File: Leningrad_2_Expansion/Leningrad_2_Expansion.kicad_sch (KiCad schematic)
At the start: 2 parts, among them J1 ZX_Spectrum_Connector_48K, X6 Leningrad 2 Expansion Bus

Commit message: Updated Leningrad-2 symbol
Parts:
- X6: value Leningrad 2 Expansion Bus -> Ленинград-2 Expansion Bus
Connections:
- net D5: no longer X6.A14 (D5)
- net D6: no longer X6.A15 (D6)
- net D7: no longer X6.A16 (D7)

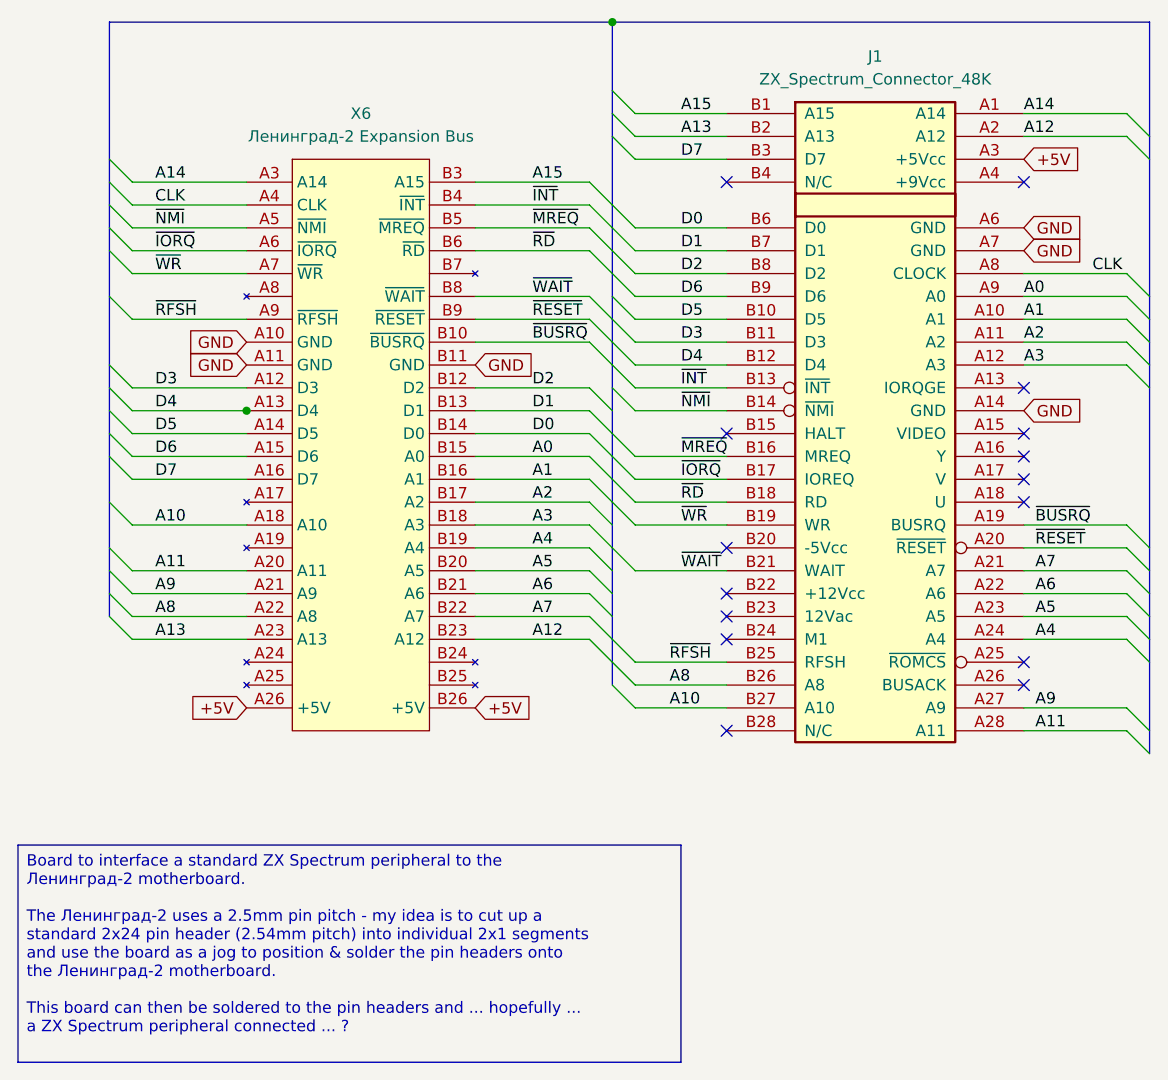
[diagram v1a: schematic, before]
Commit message: Added ~IORQGE signal
Thanks to Oleh S. suggestion on UCHC "Ukrainian Computing History Community"
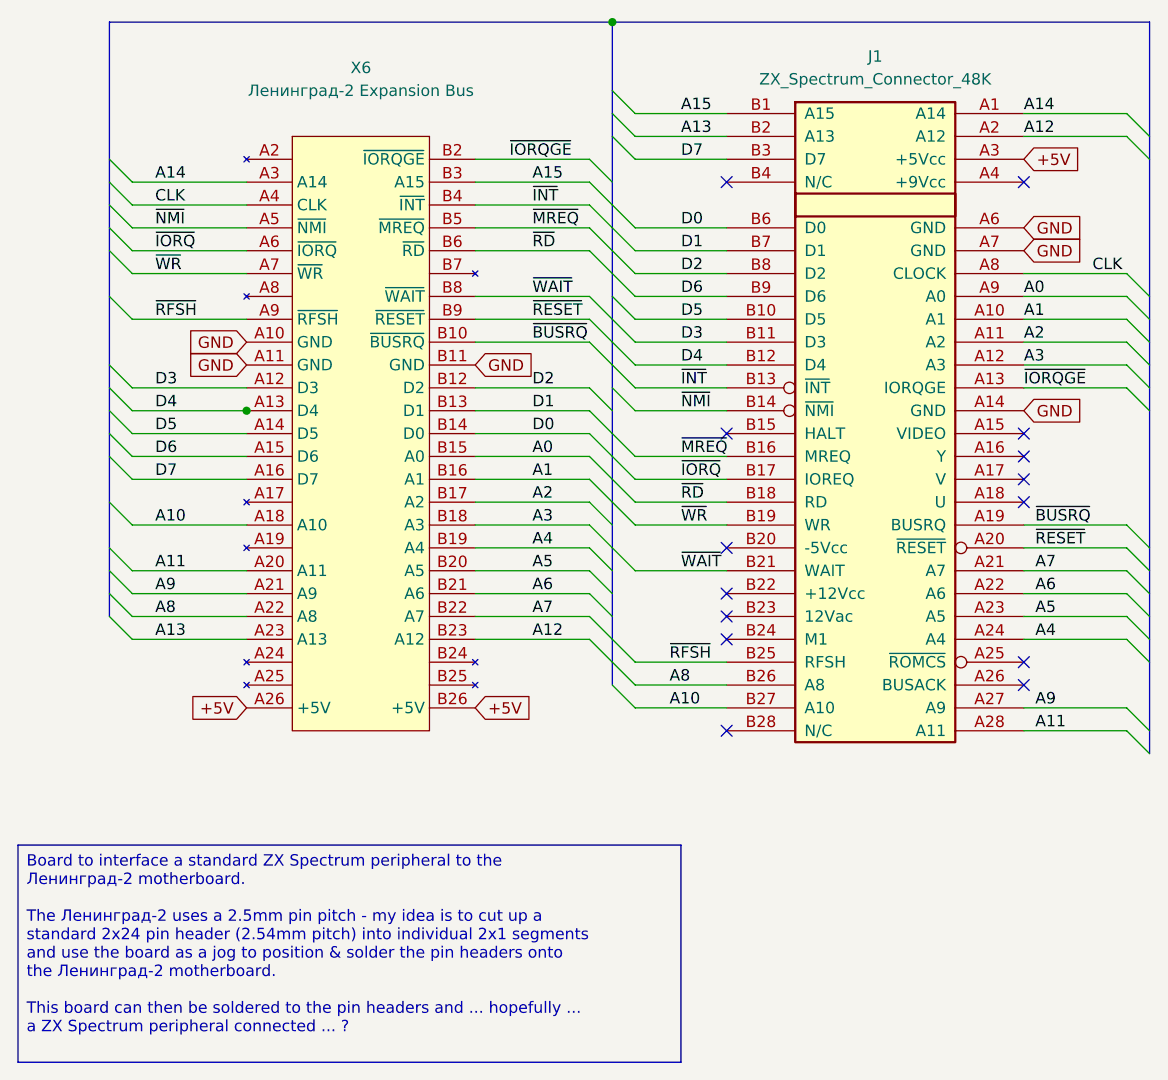
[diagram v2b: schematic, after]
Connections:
- net ~{IORQGE}: now reaches J1.A13 (IORQGE)
- net ~{IORQGE}: now also X6.B2 (~{IORQGE})
- no-connect marks 15 -> 14
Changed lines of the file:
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@@
 	(title_block
 		(title "Ленинград-2 To ZX Spectrum Bus Converter")
-		(date "16/NOV/2025")
-		(rev "A")
+		(date "17/NOV/2025")
+		(rev "B")
 		(company "Brett Hallen")
 		(comment 1 "www.youtube.com/@Brfff")
@@
 	)
 	(no_connect
-		(at 125.73 58.42)
-	)
-	(no_connect
 		(at 92.71 81.28)
 	)
@@
 	)
 	(bus_entry
+		(at 77.47 33.02)
+		(size 2.54 2.54)
+		(stroke
+			(width 0)
+			(type default)
+		)
+	)
+	(bus_entry
 		(at 80.01 43.18)
 		(size 2.54 2.54)
@@
 	)
 	(bus_entry
+		(at 137.16 58.42)
+		(size 2.54 2.54)
+		(stroke
+			(width 0)
+			(type default)
+		)
+	)
+	(bus_entry
 		(at 137.16 93.98)
 		(size 2.54 2.54)
@@
 		)
 	)
+	(bus
+		(pts
+			(xy 80.01 35.56) (xy 80.01 38.1)
+		)
+		(stroke
+			(width 0)
+			(type default)
+		)
+	)
 	(wire
 		(pts
@@
 	(wire
 		(pts
+			(xy 39.367 60.96) (xy 39.37 60.96)
+		)
+		(stroke
+			(width 0)
+			(type default)
+		)
+	)
+	(wire
+		(pts
 			(xy 125.73 45.72) (xy 137.16 45.72)
 		)
@@
 		)
 	)
+	(bus
+		(pts
+			(xy 139.7 60.96) (xy 139.7 76.2)
+		)
+		(stroke
+			(width 0)
+			(type default)
+		)
+	)
 	(wire
 		(pts
@@
 	(wire
 		(pts
-			(xy 39.367 60.96) (xy 39.37 60.96)
-		)
-		(stroke
-			(width 0)
-			(type default)
-		)
-	)
-	(wire
-		(pts
 			(xy 26.67 66.04) (xy 39.367 66.04)
 		)
@@
 		)
 	)
+	(wire
+		(pts
+			(xy 64.77 33.02) (xy 77.47 33.02)
+		)
+		(stroke
+			(width 0)
+			(type default)
+		)
+	)
 	(bus
 		(pts
@@
 	(bus
 		(pts
-			(xy 139.7 58.42) (xy 139.7 76.2)
+			(xy 139.7 58.42) (xy 139.7 60.96)
 		)
 		(stroke
@@
 		)
 	)
+	(wire
+		(pts
+			(xy 125.73 58.42) (xy 137.16 58.42)
+		)
+		(stroke
+			(width 0)
+			(type default)
+		)
+	)
 	(bus
 		(pts
@@
 	(bus
 		(pts
-			(xy 80.01 30.48) (xy 80.01 38.1)
+			(xy 80.01 30.48) (xy 80.01 35.56)
 		)
 		(stroke
@@
 	(label "A10"
 		(at 29.21 73.66 0)
+		(effects
+			(font
+				(size 1.27 1.27)
+			)
+			(justify left bottom)
+		)
+	)
+	(label "~{IORQGE}"
+		(at 125.73 58.42 0)
+		(effects
+			(font
+				(size 1.27 1.27)
+			)
+			(justify left bottom)
+		)
+	)
+	(label "~{IORQGE}"
+		(at 68.58 33.02 0)
 		(effects
 			(font
@@
 	(symbol
 		(lib_id "Clueless_Engineer:Leningrad2_Expansion")
-		(at 52.07 27.94 0)
+		(at 52.07 22.86 0)
 		(unit 1)
 		(exclude_from_sim no)
@@
 		(fields_autoplaced yes)
 		(property "Reference" "X6"
-			(at 52.07 27.94 0)
+			(at 52.07 22.86 0)
 			(effects
 				(font
@@
 		)
 		(property "Value" "Ленинград-2 Expansion Bus"
-			(at 52.07 30.48 0)
+			(at 52.07 25.4 0)
 			(effects
 				(font
@@
 		)
 		(property "Footprint" "Clueless_Engineer:Leningrad_2_Expansion_Bus"
-			(at 52.07 27.94 0)
+			(at 52.07 22.86 0)
 			(effects
 				(font
@@
 		)
 		(property "Datasheet" ""
-			(at 52.07 27.94 0)
+			(at 52.07 22.86 0)
 			(effects
 				(font
@@
 		)
 		(property "Description" "Leningrad 2 Expansion Bus"
-			(at 52.07 27.94 0)
+			(at 52.07 22.86 0)
 			(effects
 				(font
@@
 		(pin "A5"
 		)
+		(pin "B2"
+		)
+		(pin "A2"
+		)
 		(instances
-			(project ""
+			(project "Leningrad_2_Expansion"
 				(path "/948c47d7-165c-4f85-b1dd-302a4de8ae3d"
 					(reference "X6")

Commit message: PCB updates
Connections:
- net D5: now also X6.A14 (D5)
- net D6: now also X6.A15 (D6)
- net D7: now also X6.A16 (D7)
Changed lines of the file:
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@@
+	)
+	(junction
+		(at 80.01 17.78)
+		(diameter 0)
+		(color 0 0 0 0)
 	)
 	(junction
@@
 		(color 0 0 0 0)
 	)
-	(junction
-		(at 80.01 17.78)
-		(diameter 0)
-		(color 0 0 0 0)
-	)
 	(no_connect
 		(at 92.71 86.36)
@@
 	(wire
 		(pts
+			(xy 26.67 68.58) (xy 39.37 68.58)
+		)
+		(stroke
+			(width 0)
+			(type default)
+		)
+	)
+	(wire
+		(pts
 			(xy 82.55 30.48) (xy 92.71 30.48)
 		)
@@
 		)
 	)
+	(wire
+		(pts
+			(xy 26.67 66.04) (xy 39.37 66.04)
+		)
+		(stroke
+			(width 0)
+			(type default)
+		)
+	)
 	(bus
 		(pts
@@
 		)
 	)
+	(wire
+		(pts
+			(xy 26.67 63.5) (xy 39.37 63.5)
+		)
+		(stroke
+			(width 0)
+			(type default)
+		)
+	)
 	(bus
 		(pts
@@
 	(wire
 		(pts
+			(xy 26.67 60.96) (xy 39.367 60.96)
+		)
+		(stroke
+			(width 0)
+			(type default)
+		)
+	)
+	(wire
+		(pts
 			(xy 82.55 40.64) (xy 92.71 40.64)
 		)
@@
 		)
 	)
-	(wire
-		(pts
-			(xy 26.67 63.5) (xy 39.367 63.5)
-		)
-		(stroke
-			(width 0)
-			(type default)
-		)
-	)
 	(bus
 		(pts
@@
 		)
 	)
-	(wire
-		(pts
-			(xy 26.67 60.96) (xy 39.367 60.96)
-		)
-		(stroke
-			(width 0)
-			(type default)
-		)
-	)
 	(bus
 		(pts
@@
 	(wire
 		(pts
+			(xy 125.73 45.72) (xy 137.16 45.72)
+		)
+		(stroke
+			(width 0)
+			(type default)
+		)
+	)
+	(bus
+		(pts
+			(xy 139.7 60.96) (xy 139.7 76.2)
+		)
+		(stroke
+			(width 0)
+			(type default)
+		)
+	)
+	(wire
+		(pts
+			(xy 64.77 71.12) (xy 77.47 71.12)
+		)
+		(stroke
+			(width 0)
+			(type default)
+		)
+	)
+	(bus
+		(pts
+			(xy 24.13 43.18) (xy 24.13 40.64)
+		)
+		(stroke
+			(width 0)
+			(type default)
+		)
+	)
+	(wire
+		(pts
+			(xy 125.73 96.52) (xy 137.16 96.52)
+		)
+		(stroke
+			(width 0)
+			(type default)
+		)
+	)
+	(bus
+		(pts
+			(xy 24.13 66.04) (xy 24.13 71.12)
+		)
+		(stroke
+			(width 0)
+			(type default)
+		)
+	)
+	(wire
+		(pts
+			(xy 125.73 81.28) (xy 137.16 81.28)
+		)
+		(stroke
+			(width 0)
+			(type default)
+		)
+	)
+	(wire
+		(pts
+			(xy 125.73 78.74) (xy 137.16 78.74)
+		)
+		(stroke
+			(width 0)
+			(type default)
+		)
+	)
+	(bus
+		(pts
+			(xy 80.01 78.74) (xy 80.01 81.28)
+		)
+		(stroke
+			(width 0)
+			(type default)
+		)
+	)
+	(wire
+		(pts
+			(xy 64.77 35.56) (xy 77.47 35.56)
+		)
+		(stroke
+			(width 0)
+			(type default)
+		)
+	)
+	(wire
+		(pts
 			(xy 39.367 60.96) (xy 39.37 60.96)
 		)
@@
 		)
 	)
-	(wire
-		(pts
-			(xy 125.73 45.72) (xy 137.16 45.72)
-		)
-		(stroke
-			(width 0)
-			(type default)
-		)
-	)
-	(bus
-		(pts
-			(xy 139.7 60.96) (xy 139.7 76.2)
-		)
-		(stroke
-			(width 0)
-			(type default)
-		)
-	)
-	(wire
-		(pts
-			(xy 64.77 71.12) (xy 77.47 71.12)
-		)
-		(stroke
-			(width 0)
-			(type default)
-		)
-	)
-	(bus
-		(pts
-			(xy 24.13 43.18) (xy 24.13 40.64)
-		)
-		(stroke
-			(width 0)
-			(type default)
-		)
-	)
-	(wire
-		(pts
-			(xy 125.73 96.52) (xy 137.16 96.52)
-		)
-		(stroke
-			(width 0)
-			(type default)
-		)
-	)
-	(bus
-		(pts
-			(xy 24.13 66.04) (xy 24.13 71.12)
-		)
-		(stroke
-			(width 0)
-			(type default)
-		)
-	)
-	(wire
-		(pts
-			(xy 125.73 81.28) (xy 137.16 81.28)
-		)
-		(stroke
-			(width 0)
-			(type default)
-		)
-	)
-	(wire
-		(pts
-			(xy 125.73 78.74) (xy 137.16 78.74)
-		)
-		(stroke
-			(width 0)
-			(type default)
-		)
-	)
-	(bus
-		(pts
-			(xy 80.01 78.74) (xy 80.01 81.28)
-		)
-		(stroke
-			(width 0)
-			(type default)
-		)
-	)
-	(wire
-		(pts
-			(xy 64.77 35.56) (xy 77.47 35.56)
-		)
-		(stroke
-			(width 0)
-			(type default)
-		)
-	)
 	(bus
 		(pts
@@
 		)
 	)
-	(wire
-		(pts
-			(xy 26.67 66.04) (xy 39.367 66.04)
-		)
-		(stroke
-			(width 0)
-			(type default)
-		)
-	)
 	(bus
 		(pts
@@
 		)
 		(stroke
-			(width 0)
-			(type default)
-		)
-	)
-	(wire
-		(pts
-			(xy 26.67 68.58) (xy 39.367 68.58)
-		)
-		(stroke
